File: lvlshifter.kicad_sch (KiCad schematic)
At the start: 3 parts, among them Q8 BSS138

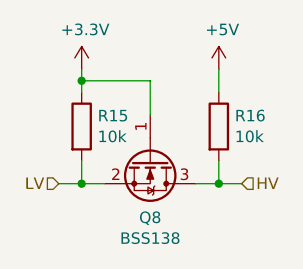
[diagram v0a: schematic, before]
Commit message: Add IBOM
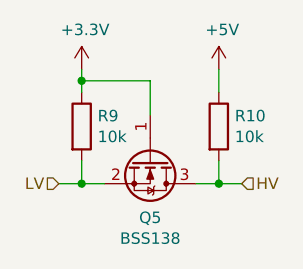
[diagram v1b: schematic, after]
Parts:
- renumbered Q8 to Q5, R16 to R10, R15 to R9
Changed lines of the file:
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@@
     (date "2021-11-03")
     (rev "v1.0a")
+    (comment 1 "Made by mole99")
   )
   (junction (at 137.16 80.01) (diameter 0) (color 0 0 0 0)
@@
   (symbol (lib_id "power:+5V") (at 152.4 78.74 0)
     (in_bom yes) (on_board yes)
-    (property "Reference" "#PWR0121" (id 0) (at 152.4 82.55 0)
+    (property "Reference" "#PWR0115" (id 0) (at 152.4 82.55 0)
       (effects (font (size 1.27 1.27)) hide)
     )
@@
   (symbol (lib_id "power:+3.3V") (at 137.16 78.74 0)
     (in_bom yes) (on_board yes)
-    (property "Reference" "#PWR0122" (id 0) (at 137.16 82.55 0)
+    (property "Reference" "#PWR0116" (id 0) (at 137.16 82.55 0)
       (effects (font (size 1.27 1.27)) hide)
     )
@@
   (symbol (lib_id "Device:R") (at 152.4 85.09 0)
     (in_bom yes) (on_board yes)
-    (property "Reference" "R16" (id 0) (at 154.178 83.9216 0)
+    (property "Reference" "R10" (id 0) (at 154.178 83.9216 0)
       (effects (font (size 1.27 1.27)) (justify left))
     )
@@
   (symbol (lib_id "Device:R") (at 137.16 85.09 0)
     (in_bom yes) (on_board yes)
-    (property "Reference" "R15" (id 0) (at 138.938 83.9216 0)
+    (property "Reference" "R9" (id 0) (at 138.938 83.9216 0)
       (effects (font (size 1.27 1.27)) (justify left))
     )
@@
   (symbol (lib_id "Transistor_FET:BSS138") (at 144.78 88.9 270)
     (in_bom yes) (on_board yes)
-    (property "Reference" "Q8" (id 0) (at 144.78 95.2246 90))
+    (property "Reference" "Q5" (id 0) (at 144.78 95.2246 90))
     (property "Value" "BSS138" (id 1) (at 144.78 97.536 90))
     (property "Footprint" "Package_TO_SOT_SMD:SOT-23" (id 2) (at 142.875 93.98 0)
